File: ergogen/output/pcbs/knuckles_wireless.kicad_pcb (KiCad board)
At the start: 2 copper layers, 130.3 x 107.9 mm, 152 parts

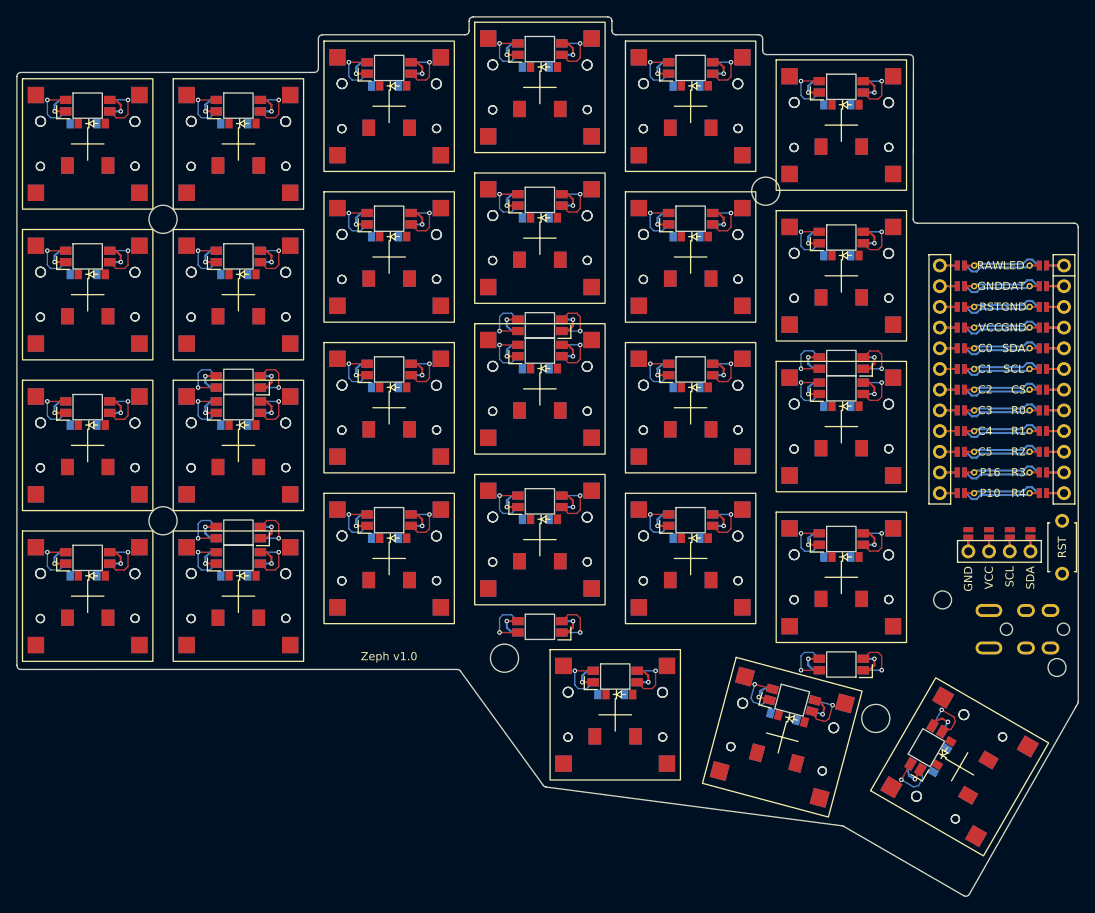
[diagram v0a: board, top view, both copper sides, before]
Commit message: feat: renamed zeph board to knuckles (#1)
* feat: renamed zeph

* fix: github action board name

* chore: more renaming
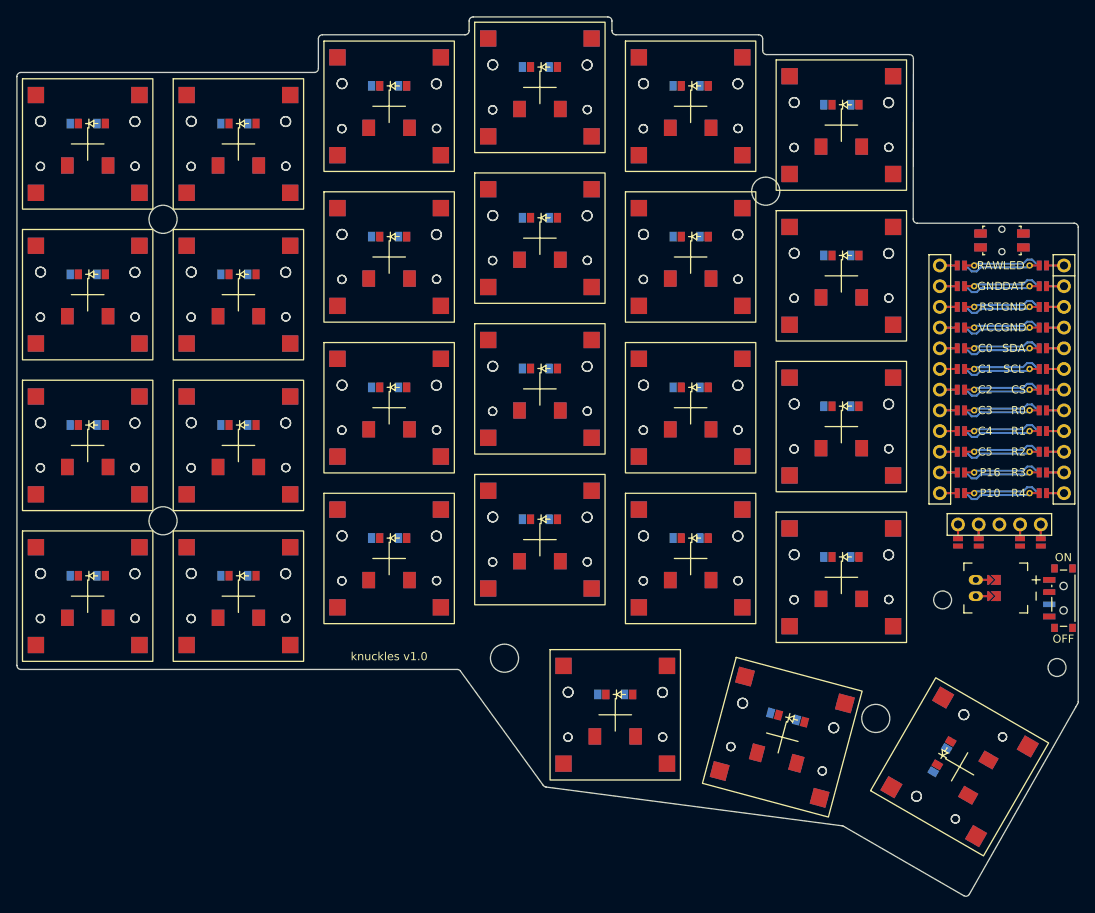
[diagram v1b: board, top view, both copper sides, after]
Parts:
- removed LED1, LED10, LED11, LED12, LED13, LED14, LED15, LED16, LED17, LED18, LED19, LED2, LED20, LED21, LED22, LED23, LED24, LED25, LED26, LED27, LED3, LED4, LED5, LED6, LED7, LED8, LED9: , ceoloide:led_SK6812mini-e (per-key, reversible)
- removed LED28, LED29, LED30, LED31, LED32, LED33: , ceoloide:led_SK6812mini-e (underglow, reversible)
- removed TRRS1: , ceoloide:trrs_pj320a (reversible, symmetric)
- added JST1: , ceoloide:battery_connector_jst_ph_2, F.Cu at (209.0, 99.0)
- added PWR1: , ceoloide:power_switch_smd_side, F.Cu at (219.8, 100.2)
- DISP1: footprint ceoloide:display_ssd1306 -> ceoloide:display_nice_view
- RST1: footprint ceoloide:reset_switch_tht_top -> ceoloide:reset_switch_smd_side
- moved RST1 38.4 mm to (212.2, 56.3), turned to 0 degrees
- moved DISP1 3.31 mm to (211.9, 74.5)
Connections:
- DISP1 pad 10: DISP1_4 -> CS
- DISP1 pad 11: DISP1_3 -> GND
- DISP1 pad 12: DISP1_2 -> SCL
- DISP1 pad 13: DISP1_1 -> SDA
- DISP1 pad 14: GND -> DISP1_1
- DISP1 pad 15: VCC -> DISP1_2
- DISP1 pad 16: SCL -> DISP1_4
- DISP1 pad 17: SDA -> DISP1_5
- DISP1 pad 20: DISP1_1 -> CS
- DISP1 pad 21: DISP1_2 -> GND
- DISP1 pad 22: DISP1_3 -> SCL
- DISP1 pad 23: DISP1_4 -> SDA
- DISP1 pad 24: GND -> DISP1_5
- DISP1 pad 25: VCC -> DISP1_4
- DISP1 pad 26: SCL -> DISP1_2
- DISP1 pad 27: SDA -> DISP1_1
- DISP1 pad 3: DISP1_3 -> VCC
- RST1 pad 1: RST -> GND
- RST1 pad 2: GND -> RST
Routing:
- net VCC: track 127.4 -> 0.00 mm, vias 33 -> 0
- net GND: track 127.4 -> 3.50 mm, vias 33 -> 0
- net (no net): track 414.2 -> 333.1 mm, vias 12 -> 0
- net ULED_5: track 13.5 -> 0.00 mm, vias 2 -> 0
- net ULED_4: track 13.5 -> 0.00 mm, vias 2 -> 0
- net ULED_3: track 13.5 -> 0.00 mm, vias 2 -> 0
- net ULED_2: track 13.5 -> 0.00 mm, vias 2 -> 0
- net ULED_1: track 13.5 -> 0.00 mm, vias 2 -> 0
- net LED_9: track 13.5 -> 0.00 mm, vias 2 -> 0
- net LED_6: track 13.5 -> 0.00 mm, vias 2 -> 0
- net LED_5: track 13.5 -> 0.00 mm, vias 2 -> 0
- net LED_4: track 13.5 -> 0.00 mm, vias 2 -> 0
- net LED_3: track 13.5 -> 0.00 mm, vias 2 -> 0
- net LED_20: track 13.5 -> 0.00 mm, vias 2 -> 0
- net LED_2: track 13.5 -> 0.00 mm, vias 2 -> 0
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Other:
- board text added: "knuckles v1.0"
- board text removed: "Zeph v1.0"
